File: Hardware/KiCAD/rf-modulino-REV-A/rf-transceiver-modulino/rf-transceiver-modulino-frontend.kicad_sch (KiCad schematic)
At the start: 86 parts, among them P1 SMA, P2 SMA, SW1 SKY13330-397LF, SW2 SKY13330-397LF, U1 CC1200RHBR, U2 LP5907MFX-2.5, U3 TXS0101DBV, X1 40 MHz

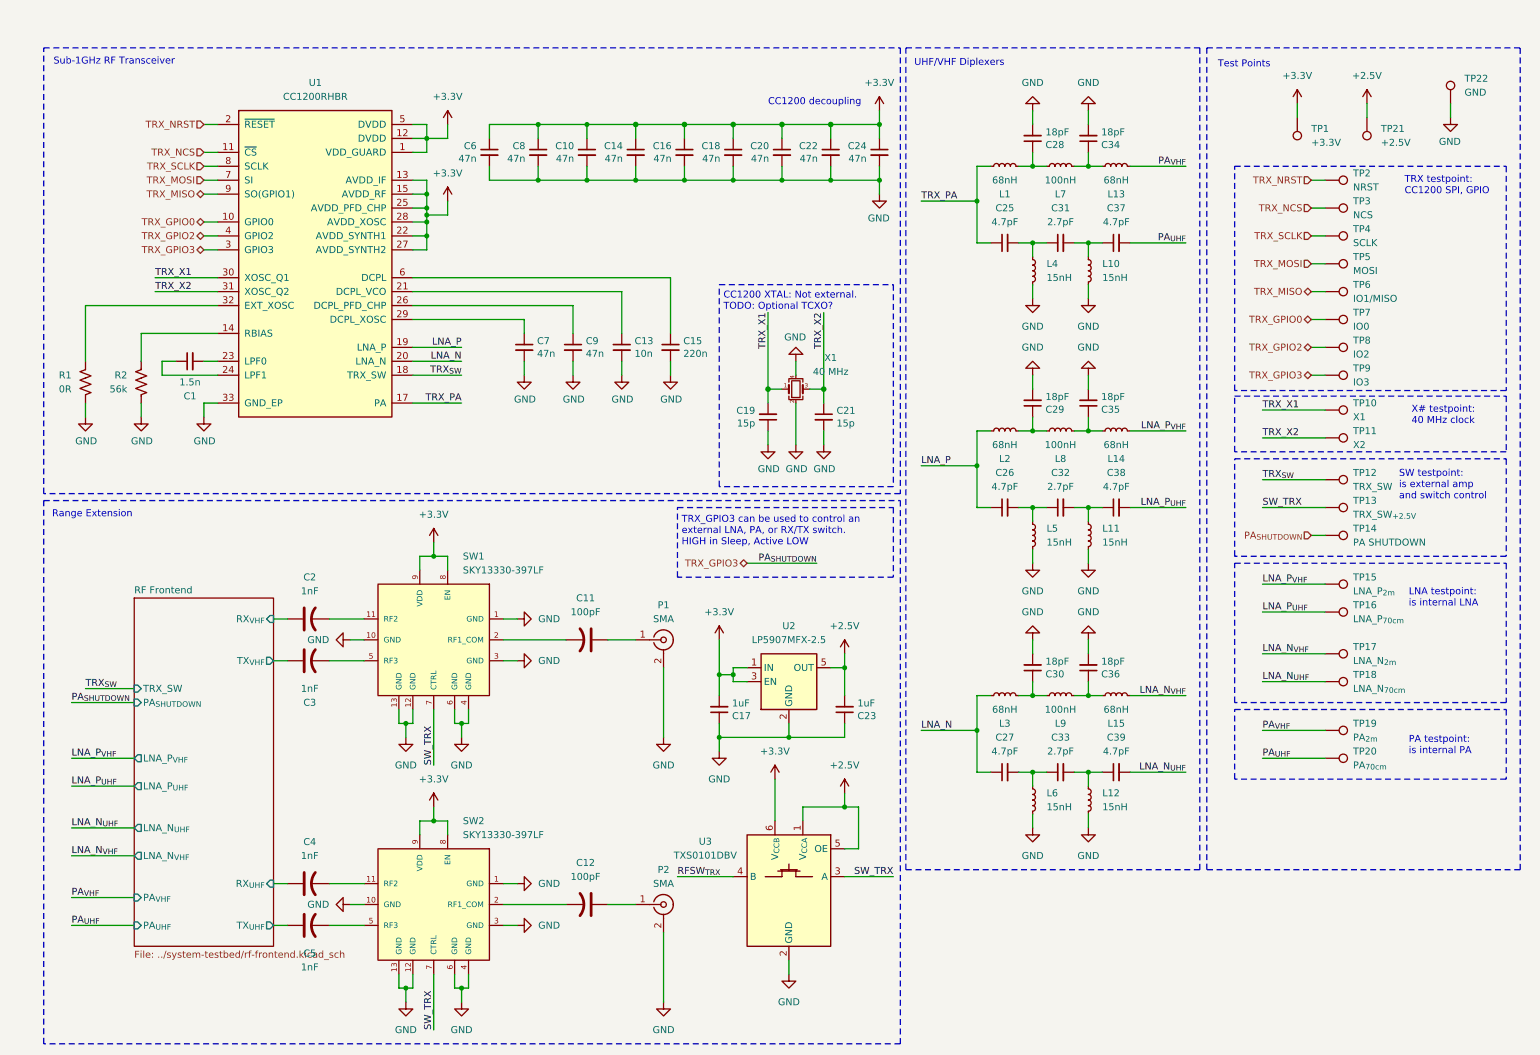
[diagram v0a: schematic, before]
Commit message: docs: update all system schematics for project uniformity
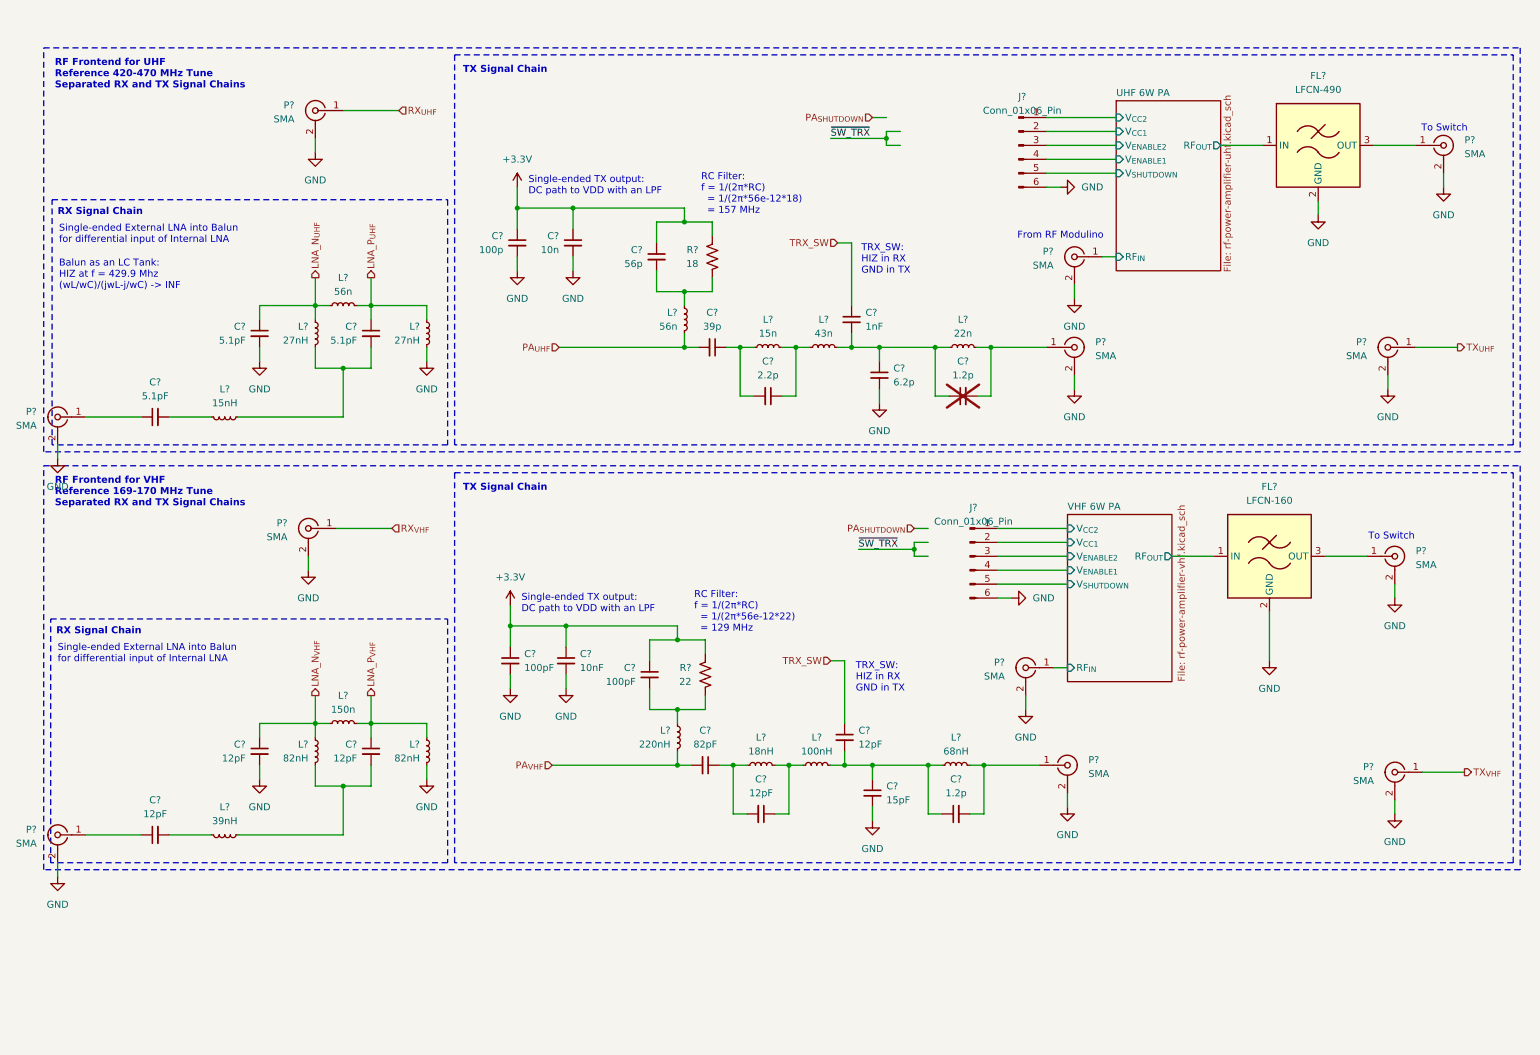
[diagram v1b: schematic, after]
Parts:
- removed C1: 1.5n, Capacitor_SMD:C_0402_1005Metric, symbol Device:C_Small
- removed C10, C14, C16, C18, C20, C22, C24, C6, C7, C8, C9: 47n, Capacitor_SMD:C_0402_1005Metric, symbol Device:C_Small
- removed C11, C12: 100pF, Capacitor_SMD:C_0402_1005Metric, symbol Device:C_US
- removed C13: 10n, Capacitor_SMD:C_0402_1005Metric, symbol Device:C_Small
- removed C15: 220n, Capacitor_SMD:C_0402_1005Metric, symbol Device:C_Small
- removed C17, C23: 1uF, Capacitor_SMD:C_0402_1005Metric, symbol Device:C_Small
- removed C19, C21: 15p, Capacitor_SMD:C_0402_1005Metric, symbol Device:C_Small
- removed C2, C3, C4, C5: 1nF, Capacitor_SMD:C_0402_1005Metric, symbol Device:C_US
- removed C25, C26, C37, C38, C39: 4.7pF, Capacitor_SMD:C_0402_1005Metric, symbol Device:C_Small
- removed C27: 4.7pF, Capacitor_SMD:C_0603_1608Metric, symbol Device:C_Small
- removed C28, C29, C30, C34, C35, C36: 18pF, Capacitor_SMD:C_0402_1005Metric, symbol Device:C_Small
- removed C31, C32, C33: 2.7pF, Capacitor_SMD:C_0402_1005Metric, symbol Device:C_Small
- removed L1, L13, L14, L15, L2, L3: 68nH, Inductor_SMD:L_0402_1005Metric, symbol Device:L_Small
- removed L10, L11, L12, L4, L5, L6: 15nH, Inductor_SMD:L_0402_1005Metric, symbol Device:L_Small
- removed L7, L8, L9: 100nH, Inductor_SMD:L_0402_1005Metric, symbol Device:L_Small
- removed P1, P2: SMA, Connector_Coaxial:SMA_Amphenol_901-144_Vertical, symbol Connector:Conn_Coaxial
- removed R1: 0R, Resistor_SMD:R_0402_1005Metric, symbol Device:R_US
- removed R2: 56k, Resistor_SMD:R_0402_1005Metric, symbol Device:R_US
- removed SW1, SW2: SKY13330-397LF, capstone-project:SKY13330-397LF, symbol capstone-project:SKY13330-397LF
- removed TP1: +3.3V, TestPoint:TestPoint_Pad_D1.0mm, symbol Connector:TestPoint
- removed TP10: X1, TestPoint:TestPoint_Pad_D1.0mm, symbol Connector:TestPoint
- removed TP11: X2, TestPoint:TestPoint_Pad_D1.0mm, symbol Connector:TestPoint
- removed TP12: TRX_SW, TestPoint:TestPoint_Pad_D1.0mm, symbol Connector:TestPoint
- removed TP13: TRX_SW_{+2.5V}, TestPoint:TestPoint_Pad_D1.0mm, symbol Connector:TestPoint
- removed TP14: PA SHUTDOWN, TestPoint:TestPoint_Pad_D1.0mm, symbol Connector:TestPoint
- removed TP15: LNA_P_{2m}, TestPoint:TestPoint_Pad_D1.0mm, symbol Connector:TestPoint
- removed TP16: LNA_P_{70cm}, TestPoint:TestPoint_Pad_D1.0mm, symbol Connector:TestPoint
- removed TP17: LNA_N_{2m}, TestPoint:TestPoint_Pad_D1.0mm, symbol Connector:TestPoint
- removed TP18: LNA_N_{70cm}, TestPoint:TestPoint_Pad_D1.0mm, symbol Connector:TestPoint
- removed TP19: PA_{2m}, TestPoint:TestPoint_Pad_D1.0mm, symbol Connector:TestPoint
- removed TP2: NRST, TestPoint:TestPoint_Pad_D1.0mm, symbol Connector:TestPoint
- removed TP20: PA_{70cm}, TestPoint:TestPoint_Pad_D1.0mm, symbol Connector:TestPoint
- removed TP21: +2.5V, TestPoint:TestPoint_Pad_D1.0mm, symbol Connector:TestPoint
- removed TP22: GND, TestPoint:TestPoint_Pad_D1.0mm, symbol Connector:TestPoint
- removed TP3: NCS, TestPoint:TestPoint_Pad_D1.0mm, symbol Connector:TestPoint
- removed TP4: SCLK, TestPoint:TestPoint_Pad_D1.0mm, symbol Connector:TestPoint
- removed TP5: MOSI, TestPoint:TestPoint_Pad_D1.0mm, symbol Connector:TestPoint
- removed TP6: IO1/MISO, TestPoint:TestPoint_Pad_D1.0mm, symbol Connector:TestPoint
- removed TP7: IO0, TestPoint:TestPoint_Pad_D1.0mm, symbol Connector:TestPoint
- removed TP8: IO2, TestPoint:TestPoint_Pad_D1.0mm, symbol Connector:TestPoint
- removed TP9: IO3, TestPoint:TestPoint_Pad_D1.0mm, symbol Connector:TestPoint
- removed U1: CC1200RHBR, Package_DFN_QFN:QFN-32-1EP_5x5mm_P0.5mm_EP3.45x3.45mm, symbol RF:CC1200
- removed U2: LP5907MFX-2.5, Package_TO_SOT_SMD:SOT-23-5, symbol Regulator_Linear:LP5907MFX-2.5
- removed U3: TXS0101DBV, Package_TO_SOT_SMD:SOT-23-6, symbol Logic_LevelTranslator:TXS0101DBV
- removed X1: 40 MHz, Crystal:Crystal_SMD_3225-4Pin_3.2x2.5mm, symbol Device:Crystal_GND24_Small
- added C?: 39p, Capacitor_SMD:C_0402_1005Metric, symbol Device:C_Small
- added C? (x2): 1.2p, Capacitor_SMD:C_0402_1005Metric, symbol Device:C_Small
- added C? (x5): 12pF, Capacitor_SMD:C_0402_1005Metric, symbol Device:C_Small
- added C?: 1nF, Capacitor_SMD:C_0402_1005Metric, symbol Device:C_Small
- added C?: 82pF, Capacitor_SMD:C_0402_1005Metric, symbol Device:C_Small
- added C?: 56p, Capacitor_SMD:C_0402_1005Metric, symbol Device:C_Small
- added C? (x3): 5.1pF, Capacitor_SMD:C_0402_1005Metric, symbol Device:C_Small
- added C? (x2): 100pF, Capacitor_SMD:C_0402_1005Metric, symbol Device:C_Small
- added C?: 10nF, Capacitor_SMD:C_0402_1005Metric, symbol Device:C_Small
- added C?: 10n, Capacitor_SMD:C_0402_1005Metric, symbol Device:C_Small
- added C?: 2.2p, Capacitor_SMD:C_0402_1005Metric, symbol Device:C_Small
- added C?: 100p, Capacitor_SMD:C_0402_1005Metric, symbol Device:C_Small
- added C?: 15pF, Capacitor_SMD:C_0402_1005Metric, symbol Device:C_Small
- added C?: 6.2p, Capacitor_SMD:C_0402_1005Metric, symbol Device:C_Small
- added FL?: LFCN-490, Filter:Filter_Mini-Circuits_FV1206, symbol RF_Filter:LFCN-490
- added FL?: LFCN-160, Filter:Filter_Mini-Circuits_FV1206, symbol RF_Filter:LFCN-160
- added J? (x2): Conn_01x06_Pin, Connector_PinHeader_2.54mm:PinHeader_1x06_P2.54mm_Vertical, symbol Connector:Conn_01x06_Pin
- added L?: 43n, Inductor_SMD:L_0402_1005Metric, symbol Device:L_Small
- added L? (x2): 27nH, Inductor_SMD:L_0402_1005Metric, symbol Device:L_Small
- added L?: 18nH, Inductor_SMD:L_0402_1005Metric, symbol Device:L_Small
- added L?: 100nH, Inductor_SMD:L_0402_1005Metric, symbol Device:L_Small
- added L? (x2): 82nH, Inductor_SMD:L_0402_1005Metric, symbol Device:L_Small
- added L? (x2): 56n, Inductor_SMD:L_0402_1005Metric, symbol Device:L_Small
- added L?: 150n, Inductor_SMD:L_0402_1005Metric, symbol Device:L_Small
- added L?: 39nH, Inductor_SMD:L_0402_1005Metric, symbol Device:L_Small
- added L?: 15n, Inductor_SMD:L_0402_1005Metric, symbol Device:L_Small
- added L?: 68nH, Inductor_SMD:L_0402_1005Metric, symbol Device:L_Small
- added L?: 15nH, Inductor_SMD:L_0402_1005Metric, symbol Device:L_Small
- added L?: 220nH, Capacitor_SMD:C_0402_1005Metric, symbol Device:L_Small
- added L?: 22n, Inductor_SMD:L_0402_1005Metric, symbol Device:L_Small
- added P? (x12): SMA, Connector_Coaxial:SMA_Molex_73251-1153_EdgeMount_Horizontal, symbol Connector:Conn_Coaxial
- added R?: 22, Resistor_SMD:R_0402_1005Metric, symbol Device:R_US
- added R?: 18, Resistor_SMD:R_0402_1005Metric, symbol Device:R_US
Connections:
- net +3.3V: now also C?.1, C?.1, C?.1, C?.1, C?.1, C?.1, R?.1, R?.1
- net GND: now also C?.2, C?.2, C?.2, C?.2, C?.2, C?.2, C?.2, C?.2, FL?.2 (GND), FL?.2 (GND), FL?.4 (GND), FL?.4 (GND), J?.6 (Pin_6), J?.6 (Pin_6), L?.2, L?.2, P?.2 (Ext), P?.2 (Ext), P?.2 (Ext), P?.2 (Ext), P?.2 (Ext), P?.2 (Ext), P?.2 (Ext), P?.2 (Ext), P?.2 (Ext), P?.2 (Ext), P?.2 (Ext), P?.2 (Ext)
- net LNA_N_{UHF}: now also C?.1, L?.1, L?.2
- net LNA_N_{VHF}: now also C?.1, L?.1, L?.2
- net LNA_P_{UHF}: now also C?.1, L?.1, L?.1
- net LNA_P_{VHF}: now also C?.1, L?.1, L?.1
- net PA_{UHF}: now also C?.2, L?.2
- net PA_{VHF}: now also C?.2, L?.2
- new net: C?.2, L?.1, R?.2 (x2)
- new net: C?.1, C?.2, L?.1 (x2)
- new net: C?.1, L?.1, L?.2 (x2)
- new net: C?.1, C?.1, C?.2, L?.1, L?.2 (x2)
- new net: C?.2, L?.2, P?.1 (In) (x2)
- new net: FL?.3 (OUT), P?.1 (In) (x2)
- new net: C?.2, L?.2, L?.2 (x2)
- new net: C?.2, L?.1 (x2)
- new net: C?.1, P?.1 (In) (x2)
- new net RX_{UHF}: P?.1 (In)
- new net RX_{VHF}: P?.1 (In)
- new net TRX_SW: C?.1, C?.1
- new net TX_{UHF}: P?.1 (In)
- new net TX_{VHF}: P?.1 (In)
- new net UHF 6W PA/RF_{IN}: P?.1 (In)
- new net UHF 6W PA/RF_{OUT}: FL?.1 (IN)
- new net UHF 6W PA/V_{CC1}: J?.2 (Pin_2)
- new net UHF 6W PA/V_{CC2}: J?.1 (Pin_1)
- new net UHF 6W PA/V_{ENABLE1}: J?.4 (Pin_4)
- new net UHF 6W PA/V_{ENABLE2}: J?.3 (Pin_3)
- new net UHF 6W PA/V_{SHUTDOWN}: J?.5 (Pin_5)
- new net VHF 6W PA/RF_{IN}: P?.1 (In)
- new net VHF 6W PA/RF_{OUT}: FL?.1 (IN)
- new net VHF 6W PA/V_{CC1}: J?.2 (Pin_2)
- new net VHF 6W PA/V_{CC2}: J?.1 (Pin_1)
- new net VHF 6W PA/V_{ENABLE1}: J?.4 (Pin_4)
- new net VHF 6W PA/V_{ENABLE2}: J?.3 (Pin_3)
- new net VHF 6W PA/V_{SHUTDOWN}: J?.5 (Pin_5)
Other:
- removed sheet RF Frontend
- added sheet UHF 6W PA (rf-power-amplifier-uhf.kicad_sch)
- added sheet VHF 6W PA (rf-power-amplifier-vhf.kicad_sch)
- note added: "Balun as an LC Tank: HIZ at f = 429.9 Mhz (wL/wC)/(jwL-j/wC) -> INF"
- note added: "From RF Modulino"
- note added: "RC Filter: f = 1/(2π*RC) = 1/(2π*56e-12*18) = 157 MHz"
- note added: "RC Filter: f = 1/(2π*RC) = 1/(2π*56e-12*22) = 129 MHz"
- note added: "RF Frontend for UHF Reference 420-470 MHz Tune Separated RX and TX Signal Chains"
- note added: "RF Frontend for VHF Reference 169-170 MHz Tune Separated RX and TX Signal Chains"
- note added: "RX Signal Chain"
- note added: "Single-ended External LNA into Balun for differential input of Internal LNA"
- note added: "Single-ended TX output: DC path to VDD with an LPF"
- note added: "TRX_SW: HIZ in RX GND in TX"
- note added: "TX Signal Chain"
- note added: "To Switch"
- note removed: "CC1200 XTAL: Not external. TODO: Optional TCXO?"
- note removed: "CC1200 decoupling"
- note removed: "LNA testpoint: is internal LNA"
- note removed: "PA testpoint: is internal PA"
- note removed: "Range Extension"
- note removed: "SW testpoint: is external amp and switch control"
- note removed: "Sub-1GHz RF Transceiver"
- note removed: "TRX testpoint: CC1200 SPI, GPIO"
- note removed: "TRX_GPIO3 can be used to control an external LNA, PA, or RX/TX switch. HIGH in Sleep, Active LOW"
- note removed: "Test Points"
- note removed: "UHF/VHF Diplexers"
- note removed: "X# testpoint: 40 MHz clock"
